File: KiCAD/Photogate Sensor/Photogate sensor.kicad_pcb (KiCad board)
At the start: 2 copper layers, 45 x 37.5 mm, 14 parts, among them J1 Conn_01x03_Pin, J2 Conn_01x03_Pin, Q1 Q_NMOS_GDS, U1 MCP6541

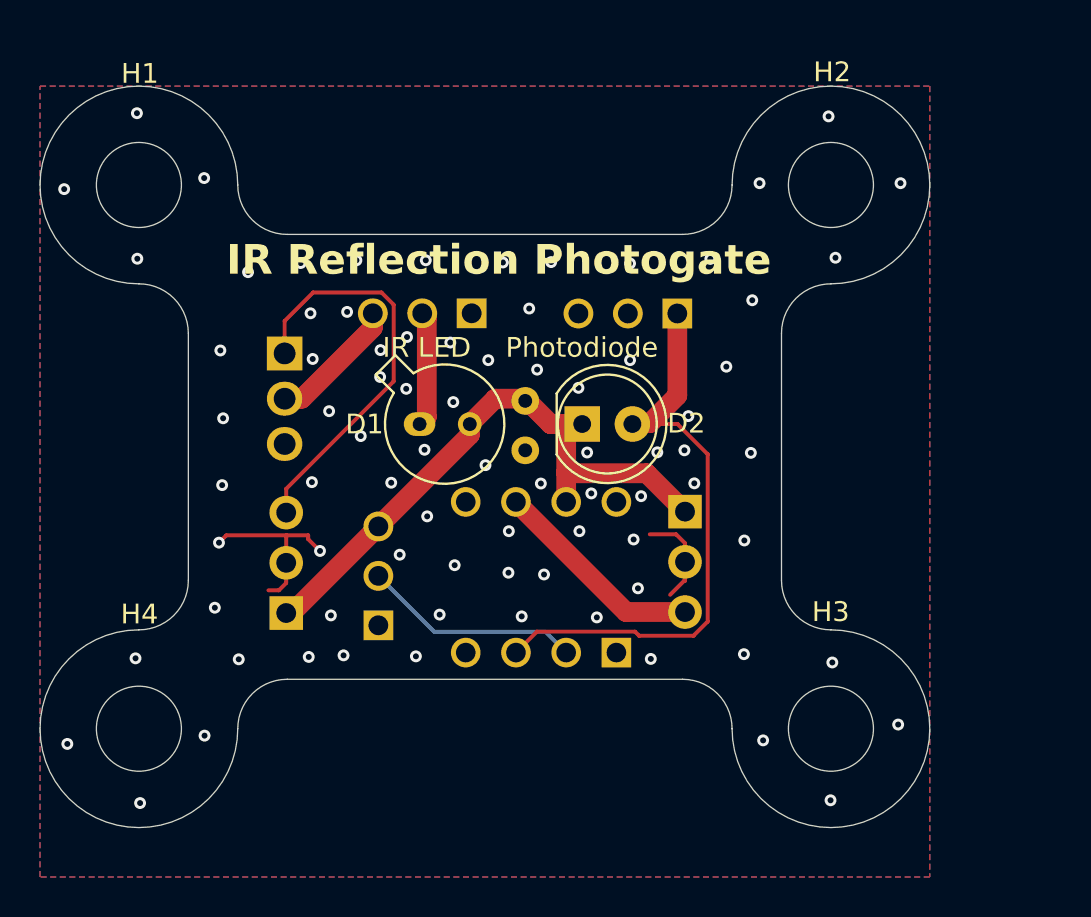
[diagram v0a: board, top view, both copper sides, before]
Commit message: Add status LED, improve traces
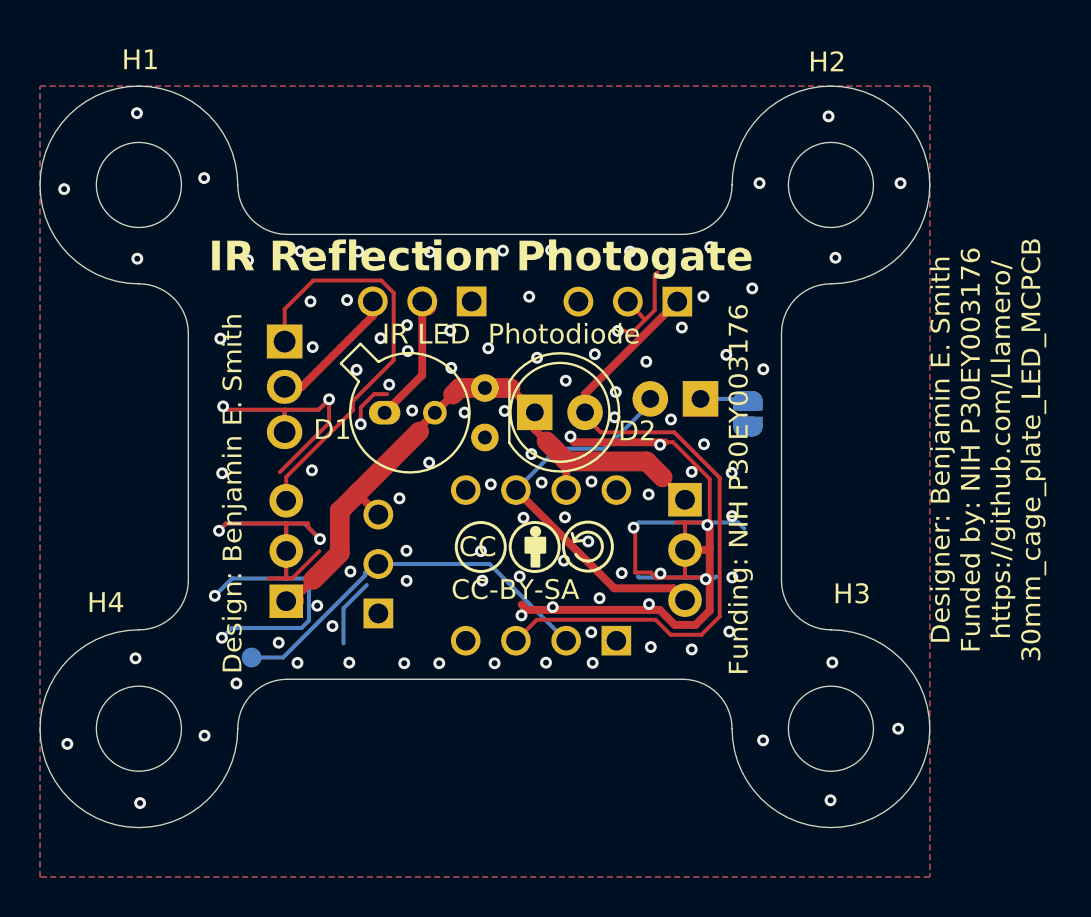
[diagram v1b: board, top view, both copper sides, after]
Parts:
- added D3: LED, LED_THT:LED_D3.0mm, B.Cu at (153.4, 85.8)
- added JP2: Jumper_2_Open, Jumper:SolderJumper-2_P1.3mm_Open_RoundedPad1.0x1.5mm, B.Cu at (155.8, 86.6)
- added SYM1: Logo_Open_Hardware_Small, Custom:CC-BY-SA Symbol, F.Cu at (145.2, 93.1)
- added TP1: TestPoint, TestPoint:TestPoint_Pad_D1.0mm, B.Cu at (130.7, 98.9)
- H1, H2, H3, H4: footprint MountingHole:MountingHole_4.3mm_M4 -> Custom:MountingHole_4.3mm_M4
- moved D2 2.47 mm to (145.0, 86.5)
- moved C1 2.14 mm to (142.5, 85.3)
- moved D1 1.86 mm to (137.4, 86.5)
- moved J1 0.60 mm to (132.4, 96.0)
- moved U1 0.60 mm to (149.2, 98.0)
- moved J2 0.60 mm to (152.6, 90.9)
- moved Q1 0.60 mm to (132.4, 82.9)
- moved RV1 0.60 mm to (149.7, 80.9)
- moved RV2 0.60 mm to (137.1, 94.2)
- moved RV3 0.60 mm to (139.3, 80.9)
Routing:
- net GND: track 14.3 -> 111.9 mm, vias 81 -> 110
- net /Trigger: track 10.9 -> 19.8 mm
- net Net-(U1-VIN-): track 11.1 -> 19.6 mm
- net /Comp+: track 30.4 -> 34.3 mm
- net Net-(D3-K): track 0.00 -> 2.44 mm
- net Net-(D1-K): track 6.04 -> 6.74 mm
- net /5V: track 31.9 -> 32.5 mm
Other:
- board text added: "+ -"
- board text added: "- +"
- board text added: "5V GND Out"
- board text added: "Design: Benjamin E. Smith"
- board text added: "Designer: Benjamin E. Smith Funded by: NIH P30EY003176 https://github.com/Llamero/ 30mm_cage_plate_LED_MCPCB"
- board text added: "Funding: NIH P30EY003176"
- board text added: "Ref"
- board text added: "Sensor LED"
- board text removed: "5V GND Trig"
